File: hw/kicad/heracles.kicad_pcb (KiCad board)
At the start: 2 copper layers, 61 parts, among them J1 USB-MICRO, K1 MOTOR_CONV, P1 LOGIC_BAT, P2 MOTOR_BAT, P3 MOTOR_A, P4 MOTOR_B, P5 CONN_8, P6 CONN_8, P7 CONN_8, P8 CONN_8, P9 CONN_8, Q1 FDV301N, Q2 FDV304P, SW1 B3U-1000P, SW2 B3U-1000P, T1 TPS62056, T2 LM3480, U1 TB6612FNG, U2 HC-05, U3 LY330ALH, U4 MMA6341L, U5 STM32F103CBT6

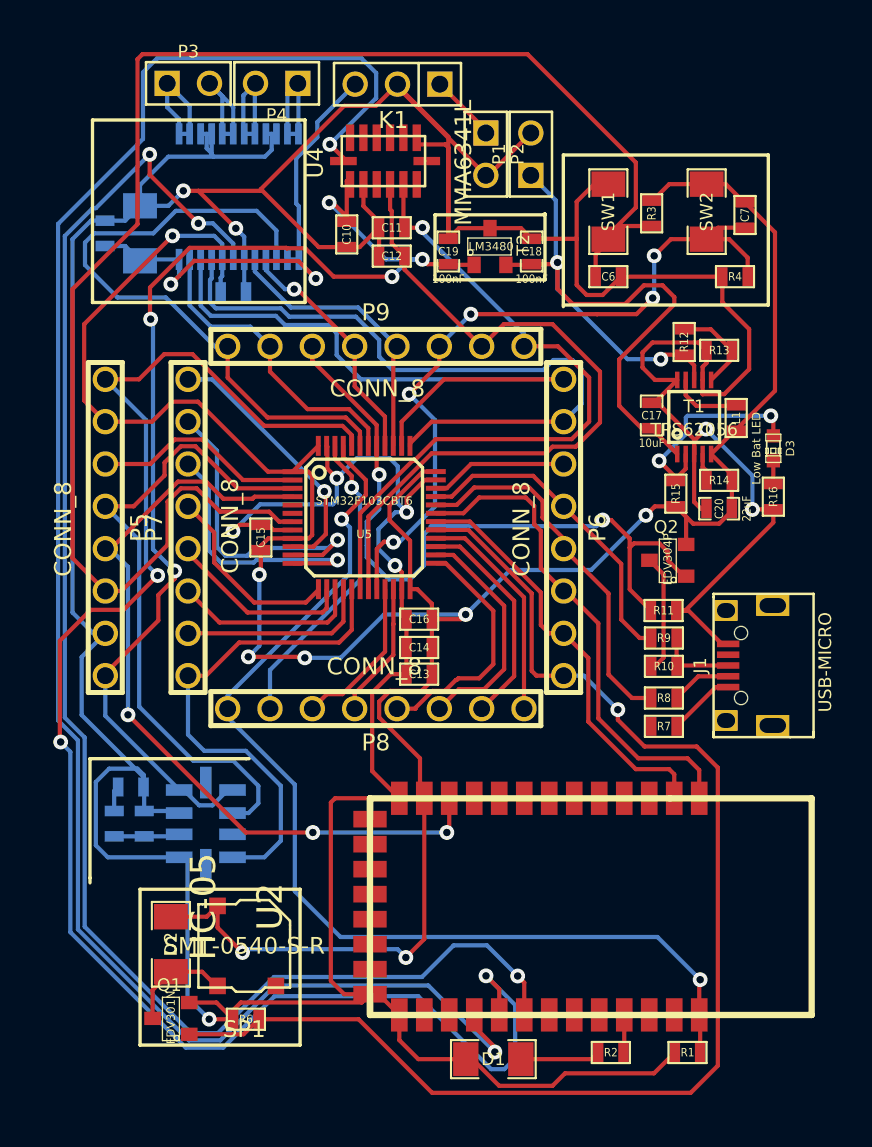
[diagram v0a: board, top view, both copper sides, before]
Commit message: Added PCB edges
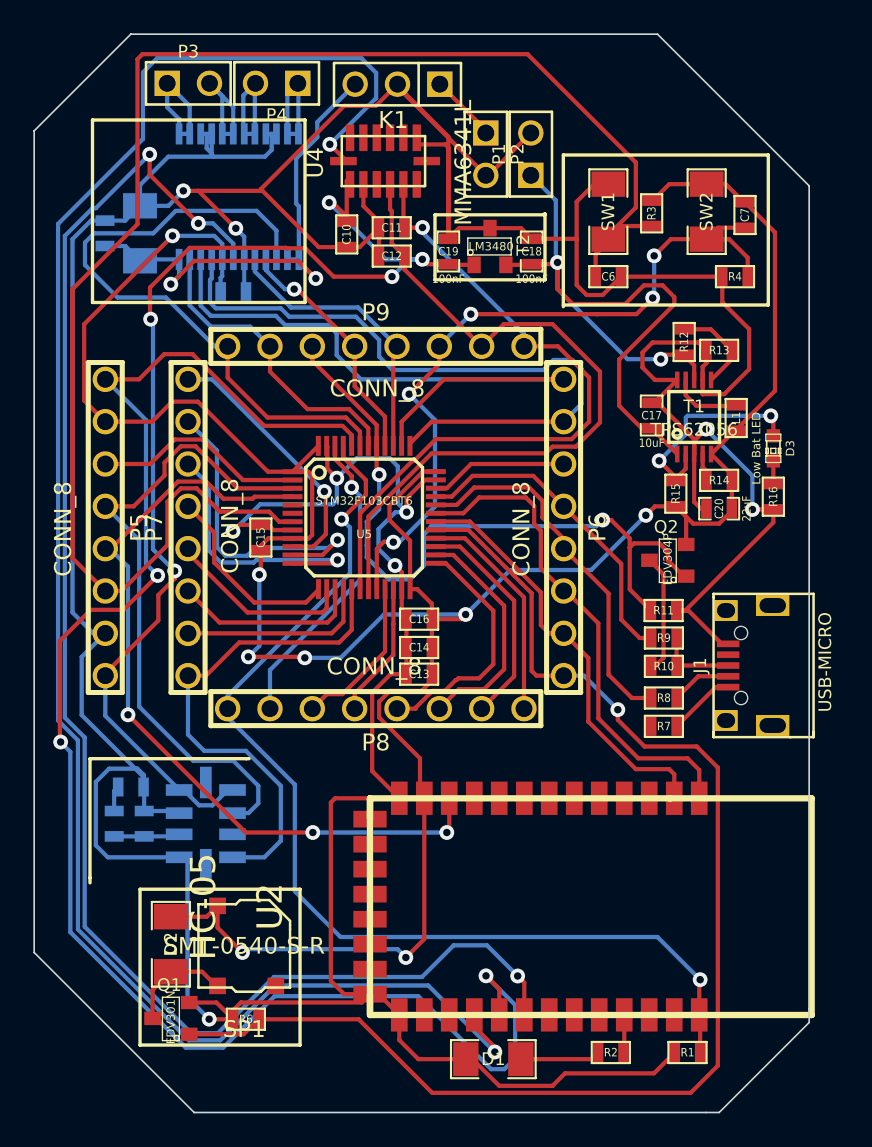
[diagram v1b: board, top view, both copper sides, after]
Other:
- board outline added: 46.5 x 64.7 mm
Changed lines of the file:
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@@
     (area 195.601 157.2338 243.0625 220.547001)
     (thickness 1.6)
-    (drawings 27)
+    (drawings 37)
     (tracks 953)
     (zones 0)
@@
     (26 Eco1.User user hide)
     (27 Eco2.User user hide)
-    (28 Edge.Cuts user hide)
+    (28 Edge.Cuts user)
   )
   (setup
@@
     )
   )
+  (gr_line (start 236 221.6) (end 235.2 221.6) (angle 90) (layer Edge.Cuts) (width 0.1))
+  (gr_line (start 241.4 216.2) (end 236 221.6) (angle 90) (layer Edge.Cuts) (width 0.1))
+  (gr_line (start 241.4 215.4) (end 241.4 216.2) (angle 90) (layer Edge.Cuts) (width 0.1))
+  (gr_line (start 241.4 215.4) (end 241.4 166) (angle 90) (layer Edge.Cuts) (width 0.1))
+  (gr_line (start 204.5 221.6) (end 235.2 221.6) (angle 90) (layer Edge.Cuts) (width 0.1))
+  (gr_line (start 200.7 156.9) (end 194.9 162.7) (angle 90) (layer Edge.Cuts) (width 0.1))
+  (gr_line (start 232.3 156.9) (end 200.7 156.9) (angle 90) (layer Edge.Cuts) (width 0.1))
+  (gr_line (start 241.4 166) (end 232.3 156.9) (angle 90) (layer Edge.Cuts) (width 0.1))
+  (gr_line (start 194.9 212) (end 204.5 221.6) (angle 90) (layer Edge.Cuts) (width 0.1))
+  (gr_line (start 194.9 162.7) (end 194.9 212) (angle 90) (layer Edge.Cuts) (width 0.1))
   (gr_line (start 211.15 173) (end 211.15 162.05) (angle 90) (layer F.SilkS) (width 0.2))
   (gr_line (start 198.4 173) (end 211.15 173) (angle 90) (layer F.SilkS) (width 0.2))
